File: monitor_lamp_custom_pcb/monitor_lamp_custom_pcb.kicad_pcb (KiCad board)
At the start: 2 copper layers, 50 x 35 mm, 39 parts, among them IC1 HUSB238, J1 USB_C_Receptacle_PowerOnly_6P, J10 Conn_01x01, J2 VEML7700_Connection, J3 LD2410C_Connection, J4 Conn_01x02, J5 SHTxx_Connection, J6 Direct_power_supply, J7 Conn_01x01, J8 Conn_01x01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

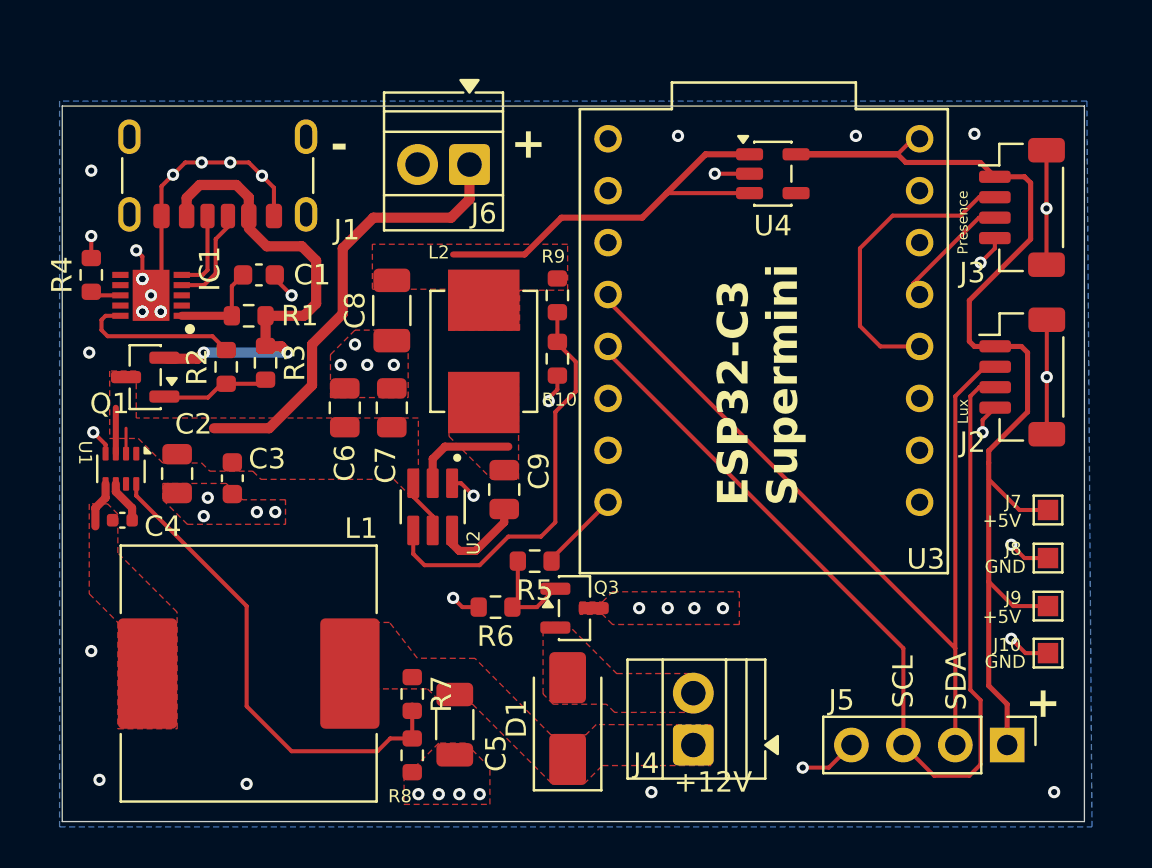
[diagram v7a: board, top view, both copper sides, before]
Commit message: Remodelled the scheme with 12V input
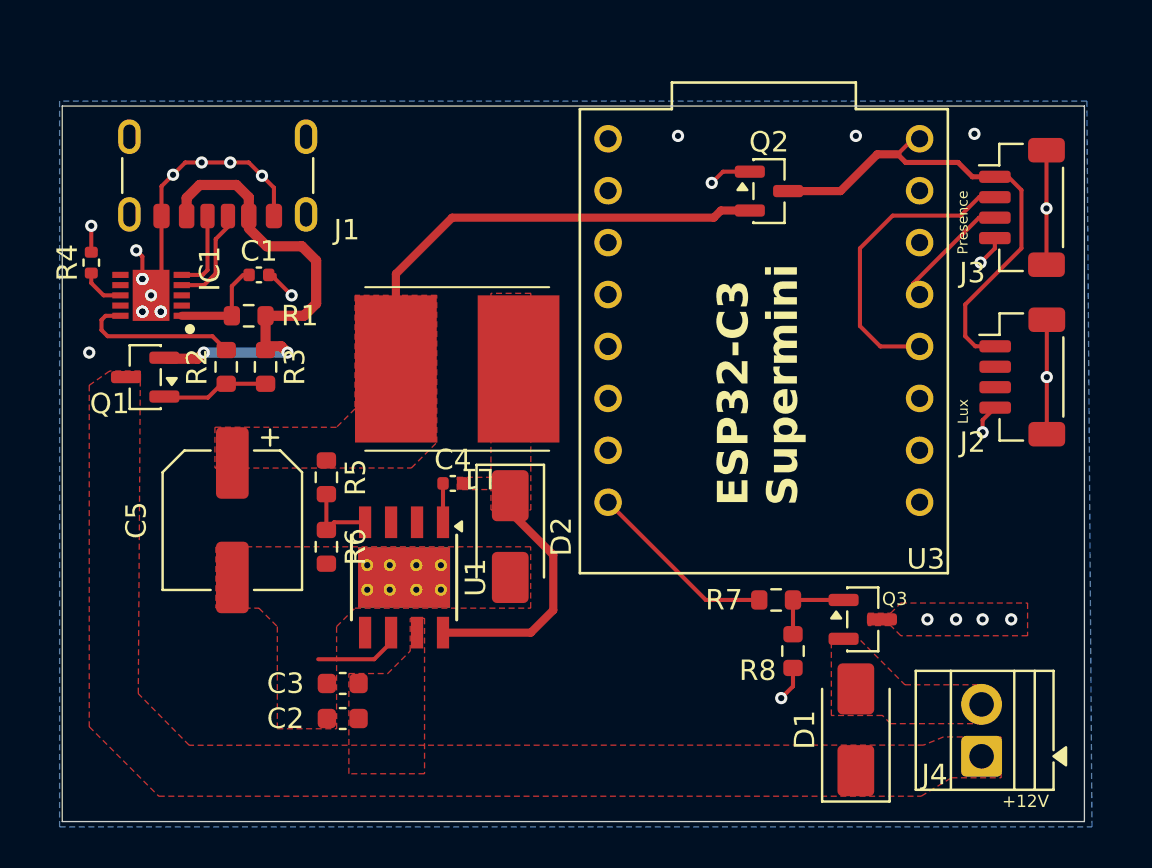
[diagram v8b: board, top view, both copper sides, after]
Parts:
- removed C6, C7: 10uF, Capacitor_SMD:C_0805_2012Metric
- removed C8: 47uF, Capacitor_SMD:C_1206_3216Metric
- removed C9: 100nF, Capacitor_SMD:C_0805_2012Metric
- removed J10, J7, J8, J9: Conn_01x01, TestPoint:TestPoint_Pad_1.0x1.0mm
- removed J5: SHTxx_Connection, Connector_PinHeader_2.54mm:PinHeader_1x04_P2.54mm_Vertical
- removed J6: Direct_power_supply, TerminalBlock:TerminalBlock_Xinya_XY308-2.54-2P_1x02_P2.54mm_Horizontal
- removed L2: 4.7uH, Inductor_SMD:L_Murata_LQH55DN_5.7x5.0mm
- removed R10: 10k, Resistor_SMD:R_0603_1608Metric
- removed R9: 54.9k, Resistor_SMD:R_0603_1608Metric
- removed U2: TPS561208DDCT, Custom_Components:SOT95P280X110-6N
- removed U4: MAX40200AUK, Package_TO_SOT_SMD:SOT-23-5
- added D2: SS14, Diode_SMD:D_SMA, F.Cu at (137.8, 74.3)
- added Q2: AO3401A, Package_TO_SOT_SMD:SOT-23, F.Cu at (150.4, 57.4)
- C1: footprint Capacitor_SMD:C_0603_1608Metric -> Capacitor_SMD:C_0402_1005Metric
- C2: footprint Capacitor_SMD:C_0805_2012Metric -> Capacitor_SMD:C_0603_1608Metric
- C3: value 100nF -> 10uF
- C4: value 100nF -> 10nF
- C5: value 10uF -> 100uF; footprint Capacitor_SMD:C_1206_3216Metric -> Capacitor_SMD:CP_Elec_6.3x5.4
- L1: value 10uH -> 68uH; footprint Inductor_SMD:L_SXN_SMDRI124 -> components:L_Sumida_CD75
- R4: value 14k -> 10k; footprint Resistor_SMD:R_0603_1608Metric -> Resistor_SMD:R_0402_1005Metric
- R5: value 22 -> 10k
- R6: value 100k -> 3.3k
- R7: value 140k -> 22
- R8: value 10k -> 100k
- U1: value TPS563300 -> TPS5430DDA; footprint Package_TO_SOT_SMD:SOT-583-8 -> Package_SO:TI_SO-PowerPAD-8_ThermalVias
- moved R8 19.3 mm to (151.6, 79.9)
- moved R7 18.4 mm to (150.8, 77.4), turned to 0 degrees
- moved L1 18.1 mm to (135.2, 66.1), turned to 180 degrees
- moved C4 16.3 mm to (135.0, 71.7), turned to 0 degrees
- moved U1 14.8 mm to (132.6, 76.3)
- moved C5 14.8 mm to (124.2, 73.5)
- moved C2 14.5 mm to (129.6, 83.2), turned to 180 degrees
- moved D1 14.1 mm to (154.7, 83.8)
- moved J4 14.1 mm to (160.8, 85.0)
- moved Q3 14.1 mm to (155.0, 78.3)
- moved C3 11.4 mm to (129.6, 81.5), turned to 180 degrees
- moved R5 11.0 mm to (128.8, 71.4), turned to -90 degrees
- moved R6 8.79 mm to (128.8, 74.8), turned to -90 degrees
- moved R4 0.60 mm to (117.3, 60.9)
- moved R3 0.20 mm to (125.8, 66.0)
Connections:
- C2 pad 1: /+15V -> /+12V
- C3 pad 1: /+15V -> /+12V
- C4 pad 1: Net-(U1-BST) -> Net-(U1-BOOT)
- C4 pad 2: Net-(U1-SW) -> Net-(D2-K)
- C5 pad 1: /+12V -> /+5V
- L1 pad 1: Net-(U1-SW) -> Net-(D2-K)
- L1 pad 2: /+12V -> /+5V
- Q1 pad 3: /+15V -> /+12V
- R5 pad 1: PWM_Control -> /+5V
- R5 pad 2: Net-(Q3-G) -> Net-(U1-VSENSE)
- R6 pad 1: Net-(Q3-G) -> Net-(U1-VSENSE)
- R7 pad 1: /+12V -> PWM_Control
- R7 pad 2: Net-(U1-FB) -> Net-(Q3-G)
- R8 pad 1: Net-(U1-FB) -> Net-(Q3-G)
- U1 pad 1: unconnected-(U1-NC-Pad1) -> Net-(U1-BOOT)
- U1 pad 2: /+15V -> unconnected-(U1-NC-Pad2)
- U1 pad 3: /+15V -> unconnected-(U1-NC-Pad3)
- U1 pad 4: GND -> Net-(U1-VSENSE)
- U1 pad 5: Net-(U1-SW) -> unconnected-(U1-EN-Pad5)
- U1 pad 6: Net-(U1-BST) -> GND
- U1 pad 7: unconnected-(U1-NC-Pad7) -> /+12V
- U1 pad 8: Net-(U1-FB) -> Net-(D2-K)
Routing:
- net /ESP32_Sensors_Mosfet/SCL: track 49.7 -> 0.00 mm
- net /ESP32_Sensors_Mosfet/SDA: track 43.9 -> 0.00 mm
- net /ESP32_Sensors_Mosfet/5V_Protected: track 53.6 -> 24.2 mm
- net /+15V: track 28.1 -> 0.00 mm
- net Net-(U1-FB): track 24.0 -> 0.00 mm
- net Net-(U2-VFB): track 20.3 -> 0.00 mm
- net Net-(D2-K): track 0.00 -> 12.3 mm
- net GND: track 46.6 -> 40.2 mm, vias 52 -> 28
- net PWM_Control: track 4.03 -> 9.37 mm
- net Net-(U2-SW): track 5.14 -> 0.00 mm
- net Net-(U2-VBST): track 4.57 -> 0.00 mm
- net Net-(U1-VSENSE): track 0.00 -> 3.80 mm
- net /+5V: track 20.6 -> 23.2 mm
- net Net-(U1-SW): track 2.28 -> 0.00 mm
- net Net-(U1-BST): track 2.11 -> 0.00 mm
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- added copper zone on F.Cu, net Net-(D2-K)
- removed copper zone on F.Cu, net /+15V
- removed copper zone on F.Cu, net Net-(U1-SW)
- removed copper zone on F.Cu, net Net-(U2-SW)
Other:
- board text removed: "+"
- board text removed: "+5V"
- board text removed: "-"
- board text removed: "GND"
- board text removed: "SCL"
- board text removed: "SDA"
